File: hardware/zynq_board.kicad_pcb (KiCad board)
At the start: 2 copper layers, 100 x 60 mm, 258 parts, among them J1 USB_OTG, J10 USB_OTG, J6 LSHM-150-xxx-x-DV-A-S, J8 Conn_01x02, J9 Micro_SD_Card_Det_Hirose_DM3AT, Q1 BSS138PS, Q2 BSS138PS, Q3 BSS138PS, U1 xc7z030sbg485, U10 TPS3808G01, U11 MT41K128M8, U13 MT41K128M8, U14 DIFF_OSC, U15 DIFF_OSC, U16 SI53340, U17 NX5P3090, U19 USB3320, U2 SFPP_CONN, U20 OSC, U21 TLK10031, U22 SN74AXC8T245, U23 SN74AXC8T245, U24 SN74AXC8T245, U25 SN74LVC2T45, U26 SN74LVC2T45, U27 SN74LVC2T45, U28 SN74LVC2T45, U29 DMF05LCFLP, U3 TPS8208x, U30 DMF05LCFLP, U31 TC1262-33, U32 MAX14854, U33 CAT24C02TDI-GT3, U34 EMIF06-MSD02N16, U37 SN74LV1T126, U38 SN74LV1T126, U4 TPS8208x, U5 TPSM84424, U6 TPSM84424, U7 TPS8208x, U8 TPS8208x, U9 TPS8208x

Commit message: Started to route DDR3 Memory.
At first added missing Footprint for Reference- and Terminationvoltage Regulator. Added Powerplanes for GND and VCCO. Added decoupling Network to both DDR3 Memory Chips. There are more small caps, to support Memory from other Manufactors.
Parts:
- removed the C142 at (186.5, 141.0)
- removed the C145 at (182.5, 141.0)
- removed D3: LED, LEDs:LED_0402
- removed the D4 at (297.7, 130.4)
- removed the J9 at (183.0, 98.8)
- removed Q2, Q3: BSS138PS, TO_SOT_Packages_SMD:SOT-363_SC-70-6
- removed the R111 at (260.2, 71.4)
- removed the R112 at (260.2, 66.8)
- removed the R113 at (246.2, 80.5)
- removed the R114 at (250.6, 75.8)
- removed R135, R137: 100k, Resistors_SMD:R_0402
- removed R136, R139: 430, Resistors_SMD:R_0402
- added C1: 47µF, Capacitors_SMD:C_1210, F.Cu at (202.2, 69.6)
- added C101: 100 nF, Capacitors_SMD:C_0201, B.Cu at (171.8, 92.6)
- added C102: 100 nF, Capacitors_SMD:C_0201, B.Cu at (174.8, 91.2)
- added C104: 100 nF, Capacitors_SMD:C_0201, B.Cu at (172.0, 98.9)
- added C106: 100 nF, Capacitors_SMD:C_0201, B.Cu at (178.8, 100.0)
- added C107: 100 nF, Capacitors_SMD:C_0201, B.Cu at (173.2, 91.2)
- added C109: 100 nF, Capacitors_SMD:C_0201, B.Cu at (176.0, 97.8)
- added C110: 100 nF, Capacitors_SMD:C_0201, B.Cu at (169.5, 99.4)
- added C111: 100 nF, Capacitors_SMD:C_0201, B.Cu at (176.0, 93.4)
- added C112: 100 nF, Capacitors_SMD:C_0201, B.Cu at (170.8, 91.2)
- added C113: 100 nF, Capacitors_SMD:C_0201, B.Cu at (174.4, 93.6)
- added C114: 10 µF, Capacitors_SMD:C_0603, F.Cu at (183.8, 110.0)
- added C115: 100 nF, Capacitors_SMD:C_0201, B.Cu at (174.8, 105.6)
- added C116: 100 nF, Capacitors_SMD:C_0201, B.Cu at (178.8, 105.6)
- added C117: 100 nF, Capacitors_SMD:C_0201, B.Cu at (173.2, 105.6)
- added C118: 100 nF, Capacitors_SMD:C_0201, B.Cu at (180.4, 105.6)
- added C119: 100 nF, Capacitors_SMD:C_0201, B.Cu at (170.8, 105.6)
- added C120: 100 nF, Capacitors_SMD:C_0201, B.Cu at (176.0, 113.4)
- added C121: 100 nF, Capacitors_SMD:C_0201, B.Cu at (172.0, 113.3)
- added C122: 100 nF, Capacitors_SMD:C_0201, B.Cu at (176.0, 107.8)
- added C123: 100 nF, Capacitors_SMD:C_0201, B.Cu at (168.4, 107.2)
- added C124: 100 nF, Capacitors_SMD:C_0201, B.Cu at (174.4, 108.1)
- added C125: 100 nF, Capacitors_SMD:C_0201, B.Cu at (171.8, 107.0)
- added C126: 100 nF, Capacitors_SMD:C_0201, B.Cu at (174.2, 113.0)
- added C127: 100 nF, Capacitors_SMD:C_0201, B.Cu at (170.4, 112.0)
- added C128: 100 nF, Capacitors_SMD:C_0201, B.Cu at (180.4, 114.4)
- added C129: 100 nF, Capacitors_SMD:C_0201, B.Cu at (169.6, 113.8)
- added C13: 0.47µF, Capacitors_SMD:C_0603, F.Cu at (218.1, 72.0)
- added C130: 100 nF, Capacitors_SMD:C_0201, B.Cu at (173.2, 114.4)
- added C132: 100 nF, Capacitors_SMD:C_0201, B.Cu at (171.6, 114.4)
- added C133: 10µF, Capacitors_SMD:C_0603, F.Cu at (155.3, 128.3)
- added C134: 100 nF, Capacitors_SMD:C_0201, B.Cu at (178.8, 114.4)
- added C136: 10µF, Capacitors_SMD:C_0603, F.Cu at (155.3, 129.5)
- added C137: 0.22µF, Capacitors_SMD:C_0402, F.Cu at (130.0, 145.1)
- added C139: 0.01µF, Capacitors_SMD:C_0402, B.Cu at (150.0, 114.0)
- added C14: 0.47µF, Capacitors_SMD:C_0603, F.Cu at (232.7, 67.1)
- added C140: 0.01µF, Capacitors_SMD:C_0402, B.Cu at (148.2, 98.4)
- added C15: 0.47µF, Capacitors_SMD:C_0603, F.Cu at (212.7, 76.8)
- added C16: 0.47µF, Capacitors_SMD:C_0603, F.Cu at (212.7, 72.0)
- added C17: 0.47µF, Capacitors_SMD:C_0603, F.Cu at (216.4, 62.3)
- added C18: 0.47µF, Capacitors_SMD:C_0603, F.Cu at (203.2, 82.1)
- added C19: 0.47µF, Capacitors_SMD:C_0603, F.Cu at (207.3, 75.5)
- added C20: 0.47µF, Capacitors_SMD:C_0603, F.Cu at (234.4, 72.0)
- added C21: 100µF, Capacitors_SMD:C_1210, F.Cu at (211.2, 63.0)
- added C22: 100µF, Capacitors_SMD:C_1210, F.Cu at (207.0, 69.6)
- added C221: 100 nF, Capacitors_SMD:C_0201, F.Cu at (269.5, 78.6)
- added C222: 100 nF, Capacitors_SMD:C_0201, F.Cu at (275.4, 74.1)
- added C23: 4.7µF, Capacitors_SMD:C_0805, F.Cu at (219.5, 86.5)
- added C231: 1 µF 6,3 V, Capacitors_SMD:C_0402, F.Cu at (338.5, 62.1)
- added C232: 1 µF 6,3 V, Capacitors_SMD:C_0402, F.Cu at (328.7, 78.1)
- added C24: 4.7µF, Capacitors_SMD:C_0805, F.Cu at (224.4, 81.7)
- added C241: 100 nF, Capacitors_SMD:C_0402, F.Cu at (300.8, 122.9)
- added C25: 4.7µF, Capacitors_SMD:C_0805, F.Cu at (228.9, 81.7)
- added C26: 4.7µF, Capacitors_SMD:C_0805, F.Cu at (237.9, 82.4)
- added C27: 0.47µF, Capacitors_SMD:C_0603, F.Cu at (219.5, 81.7)
- added C28: 0.47µF, Capacitors_SMD:C_0603, F.Cu at (227.3, 67.1)
- added C29: 0.47µF, Capacitors_SMD:C_0603, F.Cu at (232.7, 62.3)
- added C3: 47µF, Capacitors_SMD:C_1210, F.Cu at (197.4, 68.7)
- added C30: 0.47µF, Capacitors_SMD:C_0603, F.Cu at (218.1, 76.8)
- added C31: 0.47µF, Capacitors_SMD:C_0603, F.Cu at (223.5, 72.0)
- added C32: 100µF, Capacitors_SMD:C_1210, F.Cu at (153.7, 89.3)
- added C33: 0.47µF, Capacitors_SMD:C_0603, F.Cu at (214.0, 81.7)
- added C34: 47µF, Capacitors_SMD:C_1210, F.Cu at (197.4, 75.3)
- added C35: 0.47µF, Capacitors_SMD:C_0603, F.Cu at (209.1, 86.5)
- added C36: 4.7µF, Capacitors_SMD:C_0805, B.Cu at (157.4, 99.3)
- added C37: 4.7µF, Capacitors_SMD:C_0805, F.Cu at (242.9, 77.3)
- added C38: 0.47µF, Capacitors_SMD:C_0603, B.Cu at (157.1, 97.6)
- added C39: 47µF, Capacitors_SMD:C_1210, F.Cu at (202.2, 76.2)
- added C40: 0.47µF, Capacitors_SMD:C_0603, F.Cu at (223.5, 76.8)
- added C41: 0.47µF, Capacitors_SMD:C_0603, F.Cu at (229.0, 72.0)
- added C42: 0.47µF, Capacitors_SMD:C_0603, F.Cu at (221.9, 62.3)
- added C43: 4.7µF, Capacitors_SMD:C_0805, F.Cu at (243.8, 72.2)
- added C44: 0.47µF, Capacitors_SMD:C_0603, F.Cu at (214.5, 86.5)
- added C45: 4.7µF, Capacitors_SMD:C_0805, F.Cu at (238.4, 77.3)
- added C46: 0.47µF, Capacitors_SMD:C_0603, F.Cu at (238.2, 67.1)
- added C47: 0.47µF, Capacitors_SMD:C_0603, F.Cu at (243.6, 62.3)
- added C48: 100µF, Capacitors_SMD:C_1210, F.Cu at (206.3, 63.0)
- added C49: 0.47µF, Capacitors_SMD:C_0603, F.Cu at (229.0, 76.8)
- added C50: 0.47µF, Capacitors_SMD:C_0603, F.Cu at (203.7, 86.9)
- added C51: 4.7µF, Capacitors_SMD:C_0805, F.Cu at (233.4, 81.9)
- added C52: 0.47µF, Capacitors_SMD:C_0603, F.Cu at (192.8, 87.7)
- added C53: 0.47µF, Capacitors_SMD:C_0603, F.Cu at (197.8, 82.1)
- added C54: 100µF, Capacitors_SMD:C_1210, F.Cu at (192.6, 81.9)
- added C56: 4.7µF, Capacitors_SMD:C_0805, F.Cu at (243.1, 67.1)
- added C57: 0.47µF, Capacitors_SMD:C_0603, F.Cu at (216.4, 67.1)
- added C85: 1 µF 6.3 V, Capacitors_SMD:C_0402, F.Cu at (310.9, 92.2)
- added C86: 1 µF 6.3 V, Capacitors_SMD:C_0402, F.Cu at (302.0, 99.1)
- added C87: 10 µF, Capacitors_SMD:C_0603, F.Cu at (183.8, 95.8)
- added C89: 100 nF, Capacitors_SMD:C_0201, B.Cu at (170.4, 97.6)
- added C91: 100 nF, Capacitors_SMD:C_0201, B.Cu at (180.4, 91.2)
- added C92: 100 nF, Capacitors_SMD:C_0201, B.Cu at (168.4, 92.8)
- added C94: 100 nF, Capacitors_SMD:C_0201, B.Cu at (178.8, 91.2)
- added C95: 100 nF, Capacitors_SMD:C_0201, B.Cu at (171.6, 100.0)
- added C97: 100 nF, Capacitors_SMD:C_0201, B.Cu at (174.2, 98.7)
- added C98: 100 nF, Capacitors_SMD:C_0201, B.Cu at (173.2, 100.0)
- added C99: 100 nF, Capacitors_SMD:C_0201, B.Cu at (180.4, 100.0)
- added D1: LED_Small, LEDs:LED_0402, F.Cu at (268.6, 69.7)
- added D2: LED_Small, LEDs:LED_0402, F.Cu at (257.1, 77.4)
- added D6: 15 V, Diodes_SMD:D_SOD-123, F.Cu at (324.3, 138.0)
- added D7: TN1515-600B-TR, TO_SOT_Packages_SMD:TO-252-2, F.Cu at (100.8, 63.6)
- added F1: Fuse, Resistors_SMD:R_0402, F.Cu at (328.6, 137.4)
- added J10: DM3CS, footprints:DM3CS, F.Cu at (124.0, 103.4)
- added J12: Conn_01x02, footprints:WAGO-890-802, F.Cu at (89.7, 67.8)
- added J6: MDR20, footprints:Conn_MDR20, F.Cu at (74.5, 97.9)
- added L1: 120 Ohm @ 1Mhz, Inductors_SMD:L_0603, F.Cu at (196.9, 62.7)
- added R119: 300, Resistors_SMD:R_0402, F.Cu at (282.4, 82.0)
- added R120: 300, Resistors_SMD:R_0402, F.Cu at (286.4, 76.1)
- added R121: 200k, Resistors_SMD:R_0402, F.Cu at (282.4, 77.4)
- added R122: 200k, Resistors_SMD:R_0402, F.Cu at (293.9, 66.8)
- added R123: 1k, Resistors_SMD:R_0402, F.Cu at (298.5, 62.1)
- added R124: 1k, Resistors_SMD:R_0402, F.Cu at (275.5, 83.3)
- added R125: 1k, Resistors_SMD:R_0402, F.Cu at (289.8, 71.4)
- added R126: 1k, Resistors_SMD:R_0402, F.Cu at (271.5, 83.3)
- added R159: 40,2, Resistors_SMD:R_0402, F.Cu at (313.7, 120.0)
- added R40: 10kΩ, Resistors_SMD:R_0402, F.Cu at (162.7, 129.8)
- added R41: 10kΩ, Resistors_SMD:R_0402, F.Cu at (162.7, 128.8)
- added R78: 4k7, Resistors_SMD:R_0402, F.Cu at (349.8, 71.6)
- added R79: 4k7, Resistors_SMD:R_0402, F.Cu at (352.9, 71.6)
- added U11: MCP1700-2502E_SOT23, TO_SOT_Packages_SMD:SOT-23, F.Cu at (297.4, 93.5)
- added U13: TPS51206, footprints:TI_PWSON-N10_2.0x2.0mm, F.Cu at (159.2, 128.6)
- added U19: SMP1255PUTG, footprints:SMC_MicroDFN_1.8x2.0mm_0.4mm_Pitch, F.Cu at (290.0, 136.3)
- added U26: LSF0102, footprints:TI-DQE_PX2SON-N8_1.4x1mm_0.35mm_Pitch, F.Cu at (256.5, 80.5)
- added U27: LSF0102, footprints:TI-DQE_PX2SON-N8_1.4x1mm_0.35mm_Pitch, F.Cu at (279.4, 60.6)
- added U38: 33.333MHZ, footprints:ASDMB_2.5x2.0mm_1.65mm_pitch, F.Cu at (292.4, 125.6)
- added U39: SMP1255PUTG, footprints:SMC_MicroDFN_1.8x2.0mm_0.4mm_Pitch, F.Cu at (248.4, 103.5)
- added U40: FT234XD, Housings_DFN_QFN:DFN-12-1EP_3x3mm_Pitch0.45mm, F.Cu at (268.0, 100.0)
- C11: value 47µF -> 4.7µF; footprint Capacitors_SMD:C_1210 -> Capacitors_SMD:C_0805
- C12: value 100µF -> 0.47µF; footprint Capacitors_SMD:C_1210 -> Capacitors_SMD:C_0603
- C131: renamed from C48; moved to B.Cu
- C138: renamed from C53; moved to B.Cu
- C4, C6: value 0.47µF -> 4.7µF; footprint Capacitors_SMD:C_0603 -> Capacitors_SMD:C_0805
- C7: value 0.47µF -> 100µF; footprint Capacitors_SMD:C_0603 -> Capacitors_SMD:C_1210
- C9: value 4.7µF -> 0.47µF; footprint Capacitors_SMD:C_0805 -> Capacitors_SMD:C_0603
- J7: renamed from J6; moved to B.Cu
- Q1: value BSS138PS -> DMP3056L; footprint TO_SOT_Packages_SMD:SOT-363_SC-70-6 -> TO_SOT_Packages_SMD:SOT-23
- R115, R116: value 10k -> 420
- R117, R118: value 10k -> 300
- U35: renamed from U32; moved to B.Cu
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- renumbered C2 to C10, C44 to C100, C45 to C103, C46 to C105, C47 to C108, C50 to C135, C54 to C141, C55 to C142, C56 to C143, C57 to C144, C58 to C145, C59 to C146, C60 to C147, C61 to C148, C62 to C149, C63 to C150, C64 to C151, C65 to C152, C66 to C153, C67 to C154, C68 to C155, C69 to C156, C70 to C157, C71 to C158, C72 to C159, C73 to C160, C74 to C161, C75 to C162, C76 to C163, C77 to C164, C78 to C165, C79 to C166, C80 to C167, C81 to C168, C82 to C169, C83 to C170, C84 to C171, C85 to C172, C86 to C173, C87 to C174, C88 to C175, C89 to C176, C90 to C177, C91 to C178, C92 to C179, C93 to C180, C94 to C181, C95 to C182, C96 to C183, C97 to C184, C98 to C185, C99 to C186, C100 to C187, C101 to C188, C102 to C189, C103 to C190, C104 to C191, C105 to C192, C106 to C193, C107 to C194, C108 to C195, C109 to C196, C110 to C197, C111 to C198, C112 to C199, C113 to C200, C114 to C201, C115 to C202, C116 to C203, C117 to C204, C118 to C205, C119 to C206, C120 to C207, C121 to C208, C122 to C209, C123 to C210, C124 to C211, C125 to C212, C126 to C213, C127 to C214, C128 to C215, C129 to C216, C130 to C217, C131 to C218, C132 to C219, C133 to C220, C150 to C239, C151 to C240, C153 to C243, C154 to C244, C155 to C245, C156 to C246, C157 to C247, C158 to C248, C159 to C249, C160 to C250, C161 to C251, C3 to C5, C10 to C55, C8 to C58, C14 to C59, C15 to C60, C16 to C61, C17 to C62, C18 to C63, C19 to C64, C5 to C8, C40 to C88, C41 to C90, C42 to C93, C43 to C96, D2 to D4, J10 to J11, J8 to J9, R96 to R100, R97 to R101, R98 to R102, R99 to R103, R100 to R104, R101 to R105, R102 to R106, R103 to R107, R104 to R108, R105 to R109, R106 to R110, R107 to R111, R108 to R112, R109 to R113, R110 to R114, R138 to R142, R134 to R143, R140 to R144, R141 to R145, R142 to R146, R143 to R147, R144 to R148, R145 to R149, R146 to R150, R147 to R151, R148 to R152, R149 to R153, R150 to R154, R151 to R155, R152 to R156, R153 to R157, R154 to R158, R156 to R161, R157 to R162, R158 to R163, R159 to R164, R160 to R165, R66 to R68, R67 to R69, R68 to R70, R69 to R71, R70 to R72, R71 to R73, R72 to R74, R73 to R75, R74 to R76, R76 to R80, R77 to R81, R78 to R82, R79 to R83, R80 to R84, R81 to R85, R82 to R86, R83 to R87, R84 to R88, R85 to R89, R86 to R90, R87 to R91, R88 to R92, R89 to R93, R90 to R94, R91 to R95, R92 to R96, R93 to R97, R94 to R98, R95 to R99, U11 to U12, U13 to U14, U14 to U15, U15 to U16, U16 to U17, U17 to U18, U19 to U20, U20 to U21, U21 to U22, U22 to U23, U23 to U24, U24 to U25, U25 to U28, U26 to U29, U27 to U30, U28 to U31, U29 to U32, U30 to U33, U31 to U34, U33 to U36, U34 to U37, U37 to U41, U38 to U42
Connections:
- C10 pad 1: (no net) -> +1V0
- C10 pad 2: (no net) -> GND
- C100 pad 1: +1V5 -> VCCO_DDR
- C103 pad 1: +1V5 -> VCCO_DDR
- C105 pad 1: +1V5 -> VCCO_DDR
- C108 pad 1: +1V5 -> VCCO_DDR
- C11 pad 1: (no net) -> +1V0
- C11 pad 2: (no net) -> GND
- C12 pad 1: (no net) -> VCCO_13
- C12 pad 2: (no net) -> GND
- C131 pad 1: /DDR/VTT_REF -> /DDR/VREF
- C138 pad 1: /DDR/VTT_REF -> /DDR/VREF
- C141 pad 1: +3V3 -> VCCO_MIO0
- C142 pad 1: +3V3 -> VCCO_MIO0
- C145 pad 1: +3V3 -> VCCO_MIO0
- C148 pad 1: +3V3 -> VCCO_MIO0
- C149 pad 1: +1V8 -> VCCO_34
- C150 pad 1: +1V8 -> VCCO_34
- C151 pad 1: +3V3 -> VCCO_MIO0
- C152 pad 1: +1V8 -> VCCO_34
- C215 pad 1: +1V8 -> VCCO_34
- C216 pad 1: +1V8 -> VCCO_34
- C217 pad 1: +1V8 -> VCCO_34
- C218 pad 1: +3V3 -> VCCO_MIO0
- C219 pad 1: +3V3 -> VCCO_MIO0
- C220 pad 1: +3V3 -> VCCO_MIO0
- C239 pad 2: +3V3 -> VCCO_MIO0
- C240 pad 2: +3V3 -> VCCO_MIO0
- C250 pad 1: +3V3 -> VCCO_MIO0
- C4 pad 1: (no net) -> VCCO_13
- C4 pad 2: (no net) -> GND
- C5 pad 1: (no net) -> +1V0
- C5 pad 2: (no net) -> GND
- C55 pad 1: (no net) -> /Power/VCC_PLL
- C55 pad 2: (no net) -> GND
- C58 pad 1: (no net) -> /Power/VCC_PLL
- C58 pad 2: (no net) -> GND
- C59 pad 1: +3V3 -> VCCO_MIO0
- C6 pad 1: (no net) -> VCCO_13
- C6 pad 2: (no net) -> GND
- C60 pad 1: +3V3 -> VCCO_MIO0
- C7 pad 1: (no net) -> +1V0
- C7 pad 2: (no net) -> GND
- C8 pad 1: (no net) -> +1V0
- C8 pad 2: (no net) -> GND
- C88 pad 1: +1V5 -> VCCO_DDR
- C9 pad 1: (no net) -> VCCO_13
- C9 pad 2: (no net) -> GND
- C90 pad 1: +1V5 -> VCCO_DDR
- C93 pad 1: +1V5 -> VCCO_DDR
- C96 pad 1: +1V5 -> VCCO_DDR
- J11 pad 4: (no net) -> Net-(J11-Pad4)
- J7 pad 10: /Camera Connector/CAM_CTRL_0_N -> /Levelshifters/CAM_SPI_MISO
- J7 pad 100: /Camera Connector/D12_P -> GND
- J7 pad 12: GND -> /Levelshifters/CAM_SPI_MOSI
- J7 pad 14: /Camera Connector/D0_N -> /Camera Connector/T_EXP2_1
- J7 pad 15: +5V -> /IMU_EN_1
- J7 pad 16: /Camera Connector/D0_P -> /Camera Connector/T_EXP1_1
- J7 pad 17: /Camera Connector/IMU_SPI_EN_1 -> /IMU_EN_0
- J7 pad 18: GND -> /Camera Connector/FRAME_REQ_1
- J7 pad 19: /Camera Connector/IMU_SPI_EN_0 -> /IMU_CLK
- J7 pad 2: /Camera Connector/CAM_CLK_0_P -> /Levelshifters/CAM_RESET
- J7 pad 20: /Camera Connector/D1_N -> /Camera Connector/T_EXP2_0
- J7 pad 21: /Camera Connector/IMU_SPI_CLK -> /IMU_MOSI
- J7 pad 22: /Camera Connector/D1_P -> /Camera Connector/T_EXP1_0
- J7 pad 23: /Camera Connector/IMU_SPI_MOSI -> /IMU_MISO
- J7 pad 24: GND -> /Camera Connector/FRAME_REQ_0
- J7 pad 25: /Camera Connector/IMU_SPI_MISO -> /IMU_FRAME_GPIO0
- J7 pad 26: /Camera Connector/D2_N -> GND
- J7 pad 27: /IMU_FRAME_GPIO0 -> /IMU_INT1_GPIO1
- J7 pad 28: /Camera Connector/D2_P -> /Levelshifters/CAM1_CLK_REF
- J7 pad 29: /IMU_INT1_GPIO1 -> /IMU_INT2_GPIO2
- J7 pad 31: /IMU_INT2_GPIO2 -> /Levelshifters/CAM_SCL
- J7 pad 32: /Camera Connector/D3_N -> /Levelshifters/CAM0_CLK_REF
- J7 pad 33: GND -> /Levelshifters/CAM_SDA
- J7 pad 34: /Camera Connector/D3_P -> GND
- J7 pad 35: /Levelshifters/CAM1_CLK_REF -> GND
- J7 pad 36: GND -> /Camera Connector/CAM_CTRL_0_N
- J7 pad 37: GND -> /Camera Connector/LVDS_CLK0_P
- J7 pad 38: /Camera Connector/D4_N -> /Camera Connector/CAM_CTRL_0_P
- J7 pad 39: /Levelshifters/CAM0_CLK_REF -> /Camera Connector/LVDS_CLK0_N
- J7 pad 4: /Camera Connector/CAM_CLK_0_N -> /Levelshifters/CAM_SPI_CLK
- J7 pad 40: /Camera Connector/D4_P -> GND
- J7 pad 42: GND -> /Camera Connector/D1_N
- J7 pad 43: /Levelshifters/CAM_SCL -> /Camera Connector/D0_N
- J7 pad 44: /Camera Connector/D5_N -> /Camera Connector/D1_P
- J7 pad 45: /Levelshifters/CAM_SDA -> /Camera Connector/D0_P
- J7 pad 46: /Camera Connector/D5_P -> GND
- J7 pad 47: /Levelshifters/CAM_RESET -> GND
- J7 pad 48: GND -> /Camera Connector/D3_N
- J7 pad 49: /Levelshifters/CAM_SPI_EN_1 -> /Camera Connector/D4_N
- J7 pad 50: /Camera Connector/D6_N -> /Camera Connector/D3_P
- J7 pad 51: /Levelshifters/CAM_SPI_EN_0 -> /Camera Connector/D4_P
- J7 pad 52: /Camera Connector/D6_P -> GND
- J7 pad 53: /Levelshifters/CAM_SPI_CLK -> GND
- J7 pad 54: GND -> /Camera Connector/D2_N
- J7 pad 55: /Levelshifters/CAM_SPI_MISO -> /Camera Connector/D5_N
- J7 pad 56: /Camera Connector/D7_N -> /Camera Connector/D2_P
- J7 pad 57: /Levelshifters/CAM_SPI_MOSI -> /Camera Connector/D5_P
- J7 pad 58: /Camera Connector/D7_P -> GND
- J7 pad 59: /Camera Connector/T_EXP2_1 -> GND
- J7 pad 6: GND -> /Levelshifters/CAM_SPI_EN_1
- J7 pad 60: GND -> /Camera Connector/D7_N
- J7 pad 61: /Camera Connector/T_EXP1_1 -> /Camera Connector/CAM_CTRL_1_P
- J7 pad 62: /Camera Connector/CAM_CLK_1_P -> /Camera Connector/D7_P
- J7 pad 63: /Camera Connector/FRAME_REQ_1 -> /Camera Connector/CAM_CTRL_1_N
- J7 pad 64: /Camera Connector/CAM_CLK_1_N -> GND
- J7 pad 65: /Camera Connector/T_EXP2_0 -> GND
- J7 pad 66: GND -> /Camera Connector/LVDS_CLK1_N
- J7 pad 67: /Camera Connector/T_EXP1_0 -> /Camera Connector/D10_N
- J7 pad 68: /Camera Connector/CAM_CTRL_1_P -> /Camera Connector/LVDS_CLK1_P
- J7 pad 69: /Camera Connector/FRAME_REQ_0 -> /Camera Connector/D10_P
- J7 pad 70: /Camera Connector/CAM_CTRL_1_N -> GND
- J7 pad 72: GND -> /Camera Connector/D8_N
- J7 pad 73: /Camera Connector/LVDS_CLK1_P -> /Camera Connector/D11_N
- J7 pad 74: /Camera Connector/D8_N -> /Camera Connector/D8_P
- J7 pad 75: /Camera Connector/LVDS_CLK1_N -> /Camera Connector/D11_P
- J7 pad 76: /Camera Connector/D8_P -> GND
- J7 pad 78: GND -> /Camera Connector/D6_N
- J7 pad 79: /Camera Connector/LVDS_CLK0_P -> /Camera Connector/D13_N
- J7 pad 8: /Camera Connector/CAM_CTRL_0_P -> /Levelshifters/CAM_SPI_EN_0
- J7 pad 80: /Camera Connector/D9_N -> /Camera Connector/D6_P
- J7 pad 81: /Camera Connector/LVDS_CLK0_N -> /Camera Connector/D13_P
- J7 pad 82: /Camera Connector/D9_P -> GND
- J7 pad 84: GND -> /Camera Connector/D9_N
- J7 pad 85: /Camera Connector/D15_P -> /Camera Connector/D15_N
- J7 pad 86: /Camera Connector/D10_N -> /Camera Connector/D9_P
- J7 pad 87: /Camera Connector/D15_N -> /Camera Connector/D15_P
- J7 pad 88: /Camera Connector/D10_P -> GND
- J7 pad 90: GND -> /Camera Connector/D12_N
- J7 pad 91: /Camera Connector/D14_P -> /Camera Connector/D14_N
- J7 pad 92: /Camera Connector/D11_N -> /Camera Connector/D12_P
- J7 pad 93: /Camera Connector/D14_N -> /Camera Connector/D14_P
- J7 pad 94: /Camera Connector/D11_P -> GND
- J7 pad 96: GND -> /Camera Connector/CAM_CLK_0_N
- J7 pad 97: /Camera Connector/D13_P -> /Camera Connector/CAM_CLK_1_N
- J7 pad 98: /Camera Connector/D12_N -> /Camera Connector/CAM_CLK_0_P
- J7 pad 99: /Camera Connector/D13_N -> /Camera Connector/CAM_CLK_1_P
- Q1 pad 1: /Levelshifters/CAM_SCL_18 -> GND
- Q1 pad 2: +1V8 -> /V_IN
- Q1 pad 3: /Levelshifters/CAM_SDA -> Net-(D6-Pad1)
- R1 pad 1: +3V3 -> VCCO_MIO0
- R102 pad 1: +1V8 -> VCCO_34
- R106 pad 1: +1V8 -> VCCO_34
- R109 pad 1: +1V8 -> VCCO_34
- R113 pad 1: +1V8 -> VCCO_34
- R115 pad 1: +3V3 -> Net-(D1-Pad2)
- R115 pad 2: /Levelshifters/CAM_SCL -> Net-(R115-Pad2)
- R116 pad 1: +3V3 -> Net-(D2-Pad2)
- R116 pad 2: /Levelshifters/CAM_SDA -> Net-(R116-Pad2)
- R117 pad 1: +3V3 -> VCCO_34
- R117 pad 2: /SFP_SCL -> /Levelshifters/SFP_SCL_18
- R118 pad 1: +3V3 -> VCCO_34
- R118 pad 2: /SFP_SDA -> /Levelshifters/CAM_SCL_18
- R142 pad 1: +1V8 -> (no net)
- R143 pad 1: +3V3 -> VCCO_MIO0
- R144 pad 1: +3V3 -> VCCO_MIO0
- R145 pad 1: +3V3 -> VCCO_MIO0
- R146 pad 1: +3V3 -> VCCO_MIO0
- R147 pad 1: +3V3 -> VCCO_MIO0
- R149 pad 1: +3V3 -> VCCO_MIO0
- R151 pad 1: +3V3 -> VCCO_MIO0
- R153 pad 1: +3V3 -> VCCO_MIO0
- R155 pad 1: +3V3 -> VCCO_MIO0
- R162 pad 2: (no net) -> Net-(R162-Pad2)
- R163 pad 1: (no net) -> Net-(R163-Pad1)
- R165 pad 1: +3V3 -> VCCO_MIO0
- R3 pad 1: +3V3 -> VCCO_MIO0
- R4 pad 1: +3V3 -> VCCO_MIO0
- R6 pad 1: +3V3 -> VCCO_MIO0
- R7 pad 1: +3V3 -> VCCO_MIO0
- R70 pad 2: +3V3 -> VCCO_MIO0
- R74 pad 1: +1V8 -> VCCO_34
- R8 pad 1: +3V3 -> VCCO_MIO0
- R82 pad 1: +1V8 -> VCCO_34
- R84 pad 1: +1V8 -> VCCO_34
- R86 pad 1: +1V8 -> VCCO_34
- R88 pad 1: +1V8 -> VCCO_34
- R9 pad 1: +3V3 -> VCCO_MIO0
- R90 pad 1: +1V8 -> VCCO_34
- R92 pad 1: +1V8 -> VCCO_34
- R94 pad 1: +1V8 -> VCCO_34
- R96 pad 2: +1V8 -> VCCO_34
- R97 pad 2: +1V8 -> VCCO_34
- U1 pad A13: +3V3 -> VCCO_MIO0
- U1 pad A3: Net-(U1-PadA3) -> VCCO_34
- U1 pad A6: /Camera Connector/IMU_SPI_MISO -> /IMU_MISO
- U1 pad A7: /Camera Connector/IMU_SPI_CLK -> /IMU_CLK
- U1 pad AA13: Net-(U1-PadAA13) -> VCCO_13
- U1 pad AB20: Net-(U1-PadAA13) -> VCCO_13
- U1 pad B10: +3V3 -> VCCO_MIO0
- U1 pad B20: +3V3 -> VCCO_MIO0
- U1 pad B6: /Camera Connector/IMU_SPI_MOSI -> /IMU_MOSI
- U1 pad B7: /Camera Connector/IMU_SPI_EN_0 -> /IMU_EN_0
- U1 pad B8: /Camera Connector/IMU_SPI_EN_1 -> /IMU_EN_1
- U1 pad C17: +3V3 -> VCCO_MIO0
- U1 pad C7: Net-(U1-PadA3) -> VCCO_34
- U1 pad D14: +3V3 -> VCCO_MIO0
- U1 pad D4: Net-(U1-PadA3) -> VCCO_34
- U1 pad E1: Net-(U1-PadA3) -> VCCO_34
- U1 pad E11: +3V3 -> VCCO_MIO0
- U1 pad E21: Net-(U1-PadE21) -> VCCO_DDR
- U1 pad F16: (no net) -> /Processing System IO/CLK_33.33
- U1 pad F18: Net-(U1-PadE21) -> VCCO_DDR
- U1 pad F8: Net-(U1-PadA3) -> VCCO_34
- U1 pad G12: (no net) -> GND
- U1 pad G13: (no net) -> /Power/VCC_PLL
- U1 pad G14: (no net) -> GND
- U1 pad G5: Net-(U1-PadA3) -> VCCO_34
- U1 pad H16: (no net) -> /DDR/VREF
- U1 pad H2: Net-(U1-PadH2) -> VCCO_34
- U1 pad H22: Net-(U1-PadE21) -> VCCO_DDR
- U1 pad J19: Net-(U1-PadE21) -> VCCO_DDR
- U1 pad K11: (no net) -> GND
- U1 pad K12: (no net) -> VCCO_34
- U1 pad K14: +1V8 -> VCCO_34
- U1 pad K16: Net-(U1-PadE21) -> VCCO_DDR
- U1 pad K6: Net-(U1-PadH2) -> VCCO_34
- U1 pad L11: (no net) -> GND
- U1 pad L12: (no net) -> GND
- U1 pad L13: +1V8 -> VCCO_34
- U1 pad L3: Net-(U1-PadH2) -> VCCO_34
- U1 pad M11: (no net) -> GND
- U1 pad M12: (no net) -> GND
- U1 pad M14: +1V8 -> VCCO_34
- U1 pad M20: Net-(U1-PadE21) -> VCCO_DDR
- U1 pad N11: (no net) -> GND
- U1 pad N12: (no net) -> GND
- U1 pad N13: +1V8 -> VCCO_34
- U1 pad N17: Net-(U1-PadE21) -> VCCO_DDR
- U1 pad N7: Net-(U1-PadH2) -> VCCO_34
- U1 pad P12: +1V8 -> VCCO_34
- U1 pad P14: +1V8 -> VCCO_34
- U1 pad P16: (no net) -> /DDR/VREF
- U1 pad P4: Net-(U1-PadH2) -> VCCO_34
- U1 pad R1: Net-(U1-PadH2) -> VCCO_34
- U1 pad R11: (no net) -> VCCO_34
- U1 pad R13: +1V8 -> VCCO_34
- U1 pad R21: Net-(U1-PadE21) -> VCCO_DDR
- U1 pad T11: (no net) -> VCCO_34
- U1 pad T12: +1V8 -> VCCO_34
- U1 pad T14: (no net) -> VCCO_34
- U1 pad T15: (no net) -> VCCO_34
- U1 pad T18: Net-(U1-PadAA13) -> VCCO_13
- U1 pad T8: (no net) -> Net-(R78-Pad2)
- U1 pad T9: (no net) -> GND
- U1 pad U15: Net-(U1-PadAA13) -> VCCO_13
- U1 pad V10: (no net) -> Net-(R79-Pad2)
- U1 pad V12: Net-(U1-PadAA13) -> VCCO_13
- U1 pad V22: Net-(U1-PadE21) -> VCCO_DDR
- U1 pad W19: Net-(U1-PadAA13) -> VCCO_13
- U1 pad Y16: Net-(U1-PadAA13) -> VCCO_13
- U12 pad A1: +1V5 -> VCCO_DDR
- U12 pad A8: +1V5 -> VCCO_DDR
- U12 pad B2: +1V5 -> VCCO_DDR
- U12 pad C1: +1V5 -> VCCO_DDR
- U12 pad C9: +1V5 -> VCCO_DDR
- U12 pad D2: +1V5 -> VCCO_DDR
- U12 pad D9: +1V5 -> VCCO_DDR
- U12 pad E9: +1V5 -> VCCO_DDR
- U12 pad F1: +1V5 -> VCCO_DDR
- U12 pad G7: +1V5 -> VCCO_DDR
- U12 pad H1: /DDR/VTT_REF -> /DDR/VREF
- U12 pad H2: +1V5 -> VCCO_DDR
- U12 pad H9: +1V5 -> VCCO_DDR
- U12 pad K2: +1V5 -> VCCO_DDR
- U12 pad K8: +1V5 -> VCCO_DDR
- U12 pad M8: /DDR/VTT_REF -> /DDR/VREF
- U12 pad N1: +1V5 -> VCCO_DDR
- U12 pad N9: +1V5 -> VCCO_DDR
- U12 pad R1: +1V5 -> VCCO_DDR
- U12 pad R9: +1V5 -> VCCO_DDR
- U14 pad A1: +1V5 -> VCCO_DDR
- U14 pad A8: +1V5 -> VCCO_DDR
- U14 pad B2: +1V5 -> VCCO_DDR
- U14 pad C1: +1V5 -> VCCO_DDR
- U14 pad C9: +1V5 -> VCCO_DDR
- U14 pad D2: +1V5 -> VCCO_DDR
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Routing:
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- added copper zone on GND1.Cu, net GND
- added copper zone on GND6.Cu, net GND
- added copper zone on PWR3.Cu, net VCCO_DDR
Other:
- board size 100 x 60 mm -> 120 x 75 mm
- copper layers 2 -> 8
- net class PWR_DDR added: clearance 0.1, trace_width 0.3, via_dia 0.4, via_drill 0.2
- rule pad_to_mask_clearance: 0.2 -> 0.05
- board text added: "VDD"
- board text added: "VDDQ"

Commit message: Routed DDR3 Memory. Not length matched yet. Also V_TT and V_Ref is WIP. Changed Footprint for FPGA to match more Xilinx' Specs(and to ease routing).
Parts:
- added C252: 100 µF, Capacitors_SMD:C_1210, F.Cu at (172.4, 128.1)
- added C253: 100 µF, Capacitors_SMD:C_1210, F.Cu at (175.9, 128.1)
- added C254: 4,7 µF, Capacitors_SMD:C_0402, B.Cu at (183.0, 118.5)
- added C255: 4,7 µF, Capacitors_SMD:C_0402, F.Cu at (176.0, 121.5)
- added C256: 10 nF, Capacitors_SMD:C_0201, F.Cu at (175.0, 121.5)
- added C257: 10 nF, Capacitors_SMD:C_0201, F.Cu at (185.0, 118.5)
- added C258: 10 nF, Capacitors_SMD:C_0201, F.Cu at (185.0, 121.5)
- added C259: 10 nF, Capacitors_SMD:C_0201, F.Cu at (175.0, 118.5)
- added R166: 40.2Ω, Resistors_SMD:R_0402, F.Cu at (179.0, 118.5)
- added R167: 40.2Ω, Resistors_SMD:R_0402, F.Cu at (181.0, 121.5)
- added R168: 40.2Ω, Resistors_SMD:R_0402, F.Cu at (183.0, 121.5)
- added R43: 40.2Ω, Resistors_SMD:R_0402, B.Cu at (181.0, 118.5)
- added R44: 40.2Ω, Resistors_SMD:R_0402, F.Cu at (182.0, 118.5)
- added R45: 40.2Ω, Resistors_SMD:R_0402, B.Cu at (178.0, 118.5)
- added R46: 40.2Ω, Resistors_SMD:R_0402, B.Cu at (180.0, 118.5)
- added R47: 40.2Ω, Resistors_SMD:R_0402, B.Cu at (179.0, 118.5)
- added R48: 40.2Ω, Resistors_SMD:R_0402, B.Cu at (177.0, 118.5)
- added R49: 40.2Ω, Resistors_SMD:R_0402, F.Cu at (180.0, 118.5)
- added R50: 40.2Ω, Resistors_SMD:R_0402, F.Cu at (179.0, 121.5)
- added R51: 40.2Ω, Resistors_SMD:R_0402, B.Cu at (176.0, 118.5)
- added R52: 4.7 kΩ, Resistors_SMD:R_0402, F.Cu at (183.7, 113.3)
- added R53: 80.6Ω, Resistors_SMD:R_0402, B.Cu at (176.4, 109.9)
- added R54: 40.2Ω, Resistors_SMD:R_0402, F.Cu at (184.0, 118.5)
- added R55: 40.2Ω, Resistors_SMD:R_0402, F.Cu at (178.0, 118.5)
- added R56: 40.2Ω, Resistors_SMD:R_0402, F.Cu at (177.0, 118.5)
- added R57: 40.2Ω, Resistors_SMD:R_0402, B.Cu at (182.0, 118.5)
- added R58: 40.2Ω, Resistors_SMD:R_0402, F.Cu at (183.0, 118.5)
- added R59: 40.2Ω, Resistors_SMD:R_0402, F.Cu at (181.0, 118.5)
- added R60: 40.2Ω, Resistors_SMD:R_0402, F.Cu at (184.0, 121.5)
- added R61: 40.2Ω, Resistors_SMD:R_0402, F.Cu at (182.0, 121.5)
- added R62: 40.2Ω, Resistors_SMD:R_0402, F.Cu at (177.0, 121.5)
- added R63: 40.2Ω, Resistors_SMD:R_0402, F.Cu at (180.0, 121.5)
- added R64: 40.2Ω, Resistors_SMD:R_0402, F.Cu at (176.0, 118.5)
- added R65: 40.2Ω, Resistors_SMD:R_0402, F.Cu at (178.0, 121.5)
- added R66: 80.6Ω, Resistors_SMD:R_0402, F.Cu at (203.4, 121.4)
- added R67: 80.6Ω, Resistors_SMD:R_0402, F.Cu at (198.6, 121.4)
- added REF**: MountingHole_3.2mm_M3, Mounting_Holes:MountingHole_3.2mm_M3, F.Cu at (202.2, 97.1)
- added REF**: MountingHole_3.2mm_M3, Mounting_Holes:MountingHole_3.2mm_M3, F.Cu at (146.0, 80.0)
- added REF**: MountingHole_3.2mm_M3, Mounting_Holes:MountingHole_3.2mm_M3, F.Cu at (115.0, 80.0)
- added REF**: MountingHole_3.2mm_M3, Mounting_Holes:MountingHole_3.2mm_M3, F.Cu at (186.0, 131.0)
- added REF**: MountingHole_3.2mm_M3, Mounting_Holes:MountingHole_3.2mm_M3, F.Cu at (74.0, 131.0)
- added REF**: MountingHole_3.2mm_M3, Mounting_Holes:MountingHole_3.2mm_M3, F.Cu at (74.0, 64.0)
- added REF**: MountingHole_3.2mm_M3, Mounting_Holes:MountingHole_3.2mm_M3, F.Cu at (186.0, 64.0)
- C36, C38: moved to F.Cu
- moved R95 446.1 mm to (-169.1, 122.3)
- moved R99 442.7 mm to (-162.7, 123.1)
- moved C208 435.3 mm to (-179.3, 104.3)
- moved C203 435.0 mm to (-179.3, 113.2)
- moved C202 434.9 mm to (-173.6, 108.7)
- moved C201 434.8 mm to (-167.9, 104.3)
- moved R144 432.1 mm to (-122.6, 116.7)
- moved R159 432.1 mm to (-118.4, 118.7)
- moved R157 432.0 mm to (-114.3, 118.7)
- moved R104 432.0 mm to (-154.9, 118.6)
- moved R100 431.9 mm to (-159.1, 123.1)
- moved R90 431.9 mm to (-157.7, 108.8)
- moved R91 431.2 mm to (-165.9, 122.6)
- moved C213 430.8 mm to (-154.9, 123.3)
- moved C200 429.7 mm to (-179.3, 117.7)
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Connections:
- U1 pad M16: (no net) -> Net-(R66-Pad1)
- U1 pad N16: (no net) -> Net-(R67-Pad2)
- U12 pad A2: /DDR/DQ13 -> /DDR/DQ11
- U12 pad A3: /DDR/DQ15 -> /DDR/DQ10
- U12 pad A7: /DDR/DQ12 -> /DDR/DQ14
- U12 pad B8: /DDR/DQ14 -> /DDR/DQ9
- U12 pad C2: /DDR/DQ11 -> /DDR/DQ13
- U12 pad C3: /DDR/DQ9 -> /DDR/DQ12
- U12 pad C8: /DDR/DQ10 -> /DDR/DQ15
- U12 pad E3: /DDR/DQ0 -> /DDR/DQ6
- U12 pad F2: /DDR/DQ2 -> /DDR/DQ7
- U12 pad F8: /DDR/DQ3 -> /DDR/DQ2
- U12 pad G2: /DDR/DQ6 -> /DDR/DQ5
- U12 pad H7: /DDR/DQ7 -> /DDR/DQ0
- U12 pad H8: /DDR/DQ5 -> /DDR/DQ3
- U14 pad A2: /DDR/DQ29 -> /DDR/DQ31
- U14 pad A3: /DDR/DQ31 -> /DDR/DQ29
- U14 pad B8: /DDR/DQ30 -> /DDR/DQ27
- U14 pad C2: /DDR/DQ27 -> /DDR/DQ24
- U14 pad C3: /DDR/DQ25 -> /DDR/DQ26
- U14 pad C8: /DDR/DQ26 -> /DDR/DQ30
- U14 pad D7: /DDR/DQ24 -> /DDR/DQ25
- U14 pad E3: /DDR/DQ16 -> /DDR/DQ21
- U14 pad F2: /DDR/DQ18 -> /DDR/DQ20
- U14 pad F7: /DDR/DQ17 -> /DDR/DQ22
- U14 pad F8: /DDR/DQ19 -> /DDR/DQ18
- U14 pad G2: /DDR/DQ22 -> /DDR/DQ19
- U14 pad H3: /DDR/DQ20 -> /DDR/DQ17
- U14 pad H8: /DDR/DQ21 -> /DDR/DQ16
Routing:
- net /DDR/A8: track 0.00 -> 88.1 mm, vias 0 -> 3
- net /DDR/A13: track 0.00 -> 86.2 mm, vias 0 -> 3
- net /DDR/A7: track 0.00 -> 85.2 mm, vias 0 -> 3
- net /DDR/A5: track 0.00 -> 85.0 mm, vias 0 -> 3
- net /DDR/A2: track 0.00 -> 84.5 mm, vias 0 -> 4
- net /DDR/DDR_BA0: track 0.00 -> 83.7 mm, vias 0 -> 4
- net /DDR/A6: track 0.00 -> 83.4 mm, vias 0 -> 4
- net /DDR/A4: track 0.00 -> 83.4 mm, vias 0 -> 4
- net /DDR/A3: track 0.00 -> 83.2 mm, vias 0 -> 3
- net /DDR/A1: track 0.00 -> 82.9 mm, vias 0 -> 4
- net /DDR/A11: track 0.00 -> 81.5 mm, vias 0 -> 4
- net /DDR/DDR_BA2: track 0.00 -> 81.5 mm, vias 0 -> 4
- net /DDR/A9: track 0.00 -> 81.2 mm, vias 0 -> 3
- net /DDR/A0: track 0.00 -> 80.8 mm, vias 0 -> 4
- net /DDR/~DDR_RESET~: track 0.00 -> 80.4 mm, vias 0 -> 3
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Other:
- net class DDR_DIFF_G2 added: clearance 0.15, trace_width 0.17, via_dia 0.4, via_drill 0.2
- net class DDR_GROUP_1 added: clearance 0.1, trace_width 0.14, via_dia 0.4, via_drill 0.2
- net class DDR_GROUP_2 added: clearance 0.1, trace_width 0.205, via_dia 0.4, via_drill 0.2
- net class DDR_GROUP_3 added: clearance 0.1, trace_width 0.205, via_dia 0.4, via_drill 0.2
- net class DDR_GROUP_4 added: clearance 0.1, trace_width 0.205, via_dia 0.4, via_drill 0.2
- net class DDR_GROUP_5 added: clearance 0.1, trace_width 0.14, via_dia 0.4, via_drill 0.2
- net class PWR_FPGA added: clearance 0.1, trace_width 0.3, via_dia 0.4, via_drill 0.2

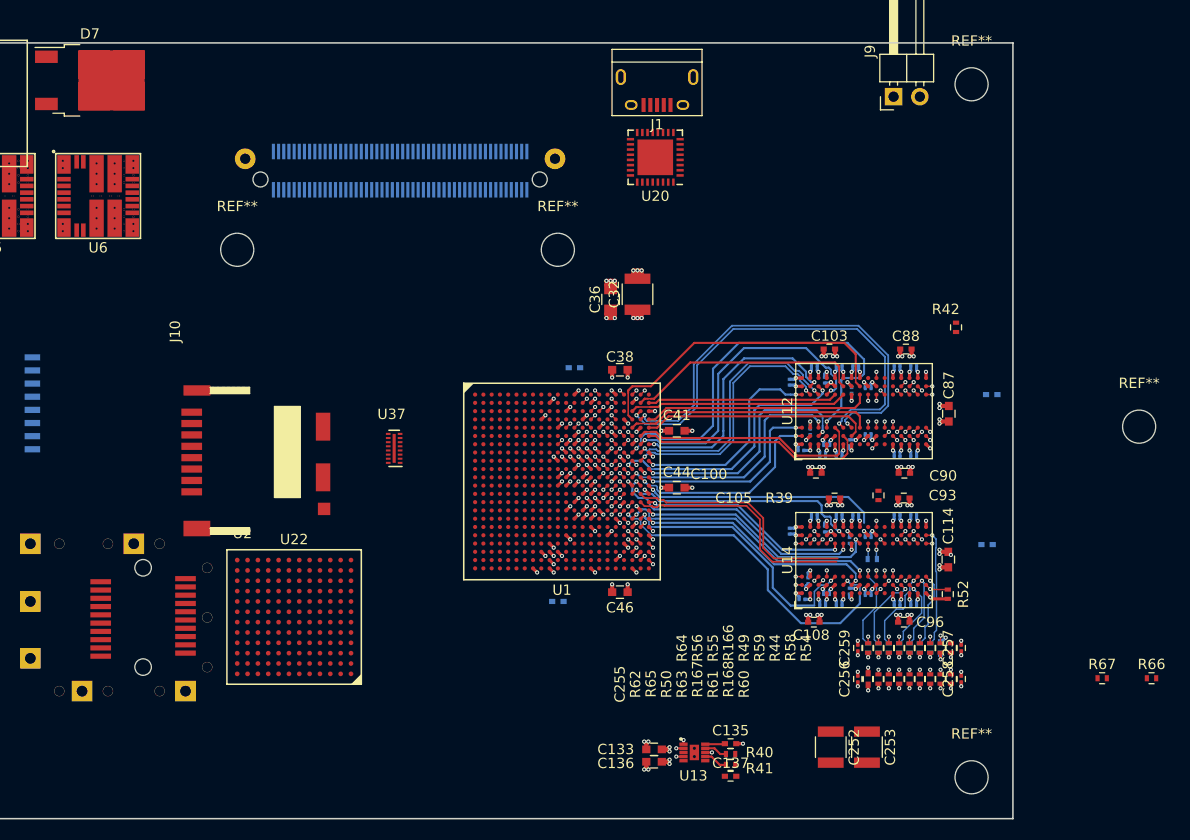
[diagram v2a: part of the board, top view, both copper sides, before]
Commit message: Connected V_TT and V_Ref. Needs to be connected to 5V.
DDR Traces are still not length matched. V_DDR supply is missing.
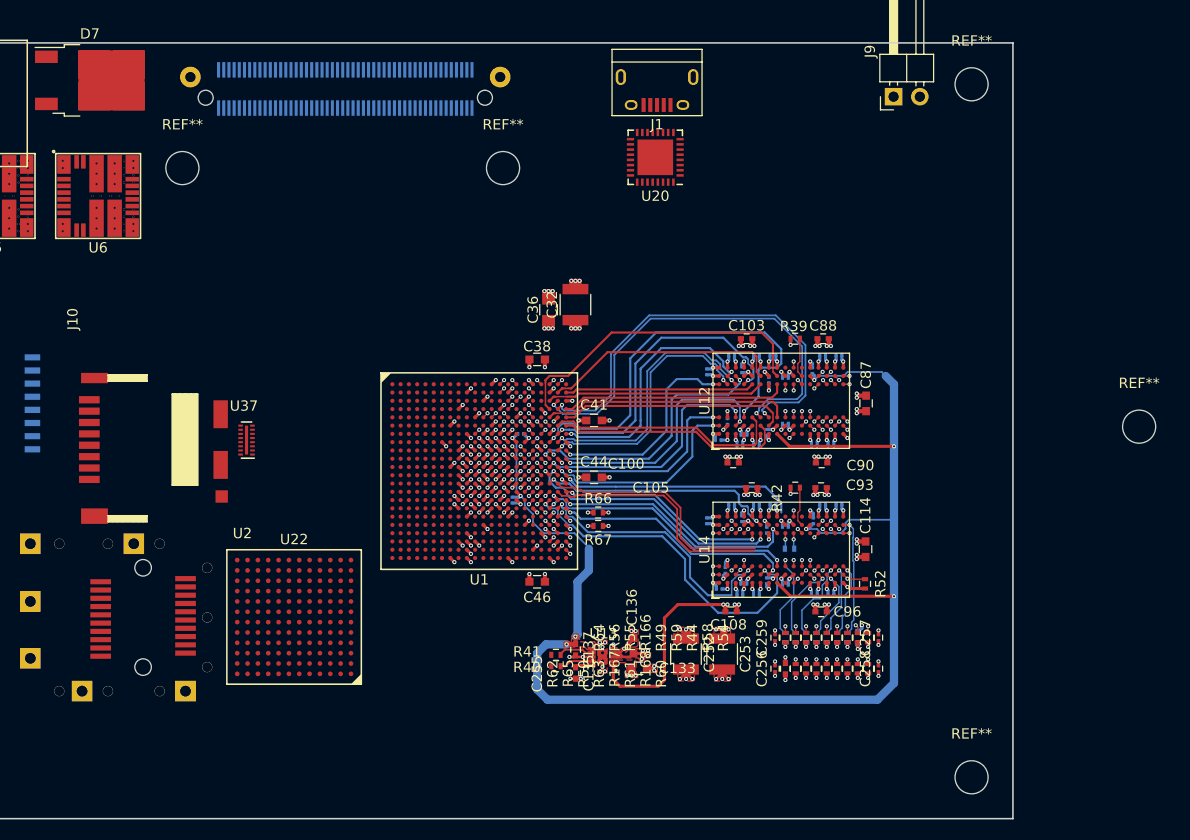
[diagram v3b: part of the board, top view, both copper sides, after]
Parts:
- C131, C138, C139, C140: footprint Capacitors_SMD:C_0402 -> Capacitors_SMD:C_0201
- moved R66 55.8 mm to (149.9, 105.4)
- moved R67 50.9 mm to (149.9, 106.7), turned to 180 degrees
- moved R42 22.0 mm to (168.9, 103.0), turned to 180 degrees
- moved R40 20.0 mm to (145.8, 119.2), turned to 180 degrees
- moved C137 19.3 mm to (147.7, 118.7), turned to 270 degrees
- moved R41 18.9 mm to (145.8, 120.3), turned to 0 degrees
- moved C138 17.5 mm to (170.6, 91.7), turned to 90 degrees
- moved R39 17.2 mm to (168.9, 88.6), turned to 180 degrees
- moved C131 17.0 mm to (170.7, 106.2), turned to 90 degrees
- moved C252 16.6 mm to (158.4, 119.1)
- moved C253 16.6 mm to (161.9, 119.1)
- moved C135 16.5 mm to (147.7, 120.9), turned to 270 degrees
- moved U37 14.3 mm to (115.9, 98.4)
- moved U13 12.8 mm to (150.3, 119.4), turned to 90 degrees
- moved C136 11.4 mm to (153.3, 118.3), turned to 270 degrees
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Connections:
- U13 pad PAD: Net-(U13-PadPAD) -> GND
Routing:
- net /DDR/VREF: track 1.13 -> 144.5 mm, vias 2 -> 8
- net GND: track 105.3 -> 133.5 mm, vias 132 -> 164
- net VCCO_DDR: track 73.1 -> 92.6 mm, vias 78 -> 79
- net /DDR/VTT: track 14.9 -> 30.2 mm, vias 24 -> 33
- net Net-(R66-Pad1): track 0.00 -> 11.9 mm, vias 0 -> 2
- net /DDR/A14: track 77.8 -> 88.8 mm, vias 3 -> 4
- net Net-(R67-Pad2): track 0.00 -> 10.9 mm, vias 0 -> 2
- net VCCO_34: track 1.13 -> 7.92 mm, vias 2 -> 14
- net +1V0: track 5.09 -> 9.05 mm, vias 9 -> 16
- net Net-(R39-Pad1): track 0.00 -> 3.85 mm
- net Net-(R42-Pad1): track 0.00 -> 3.85 mm
- net /DDR/~DDR_RESET~: track 80.4 -> 78.3 mm
- net /DDR/A13: track 86.2 -> 84.7 mm
- net /DDR/A3: track 83.2 -> 81.8 mm
- net /DDR/A7: track 85.2 -> 83.9 mm
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- added copper zone on F.Cu, net /DDR/VREF
- added copper zone on F.Cu, net /DDR/VTT
- added copper zone on PWR4.Cu, net /DDR/VTT
- added copper zone on F.Cu, net GND
- added copper zone on F.Cu, net VCCO_DDR
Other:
- board text added: "TODO: Attach 5V"
- board text removed: "VDD"
- board text removed: "VDDQ"

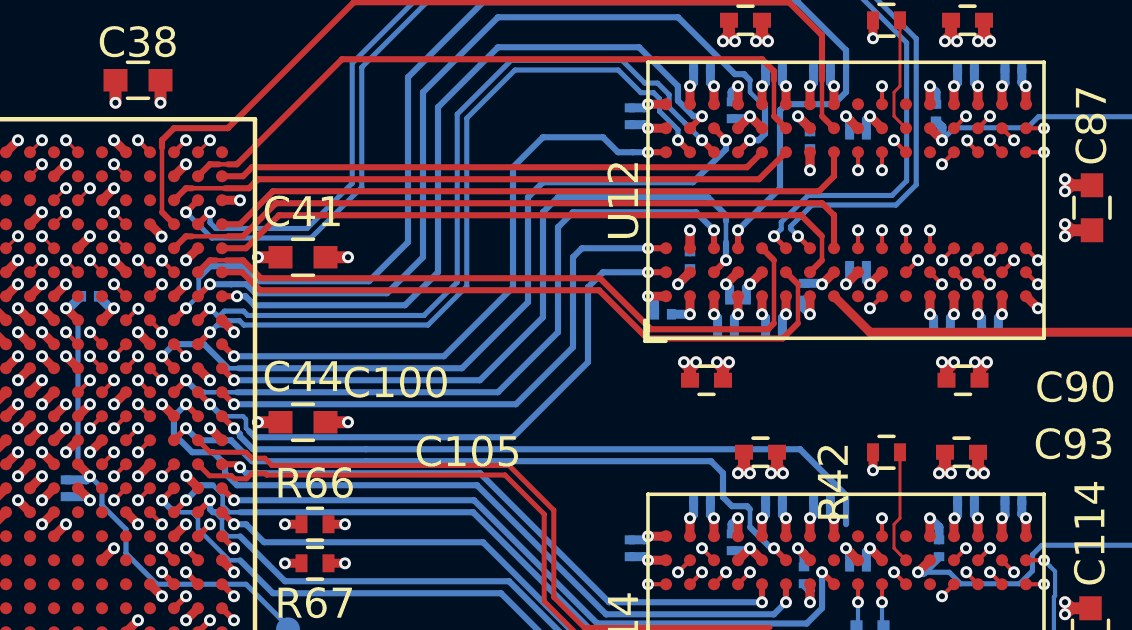
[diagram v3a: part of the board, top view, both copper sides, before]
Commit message: DDR3 Addressbus is length matched.
Databus is not length matched yet. Also DQS3 still needs to be connected. I have no good Idea for that, yet.
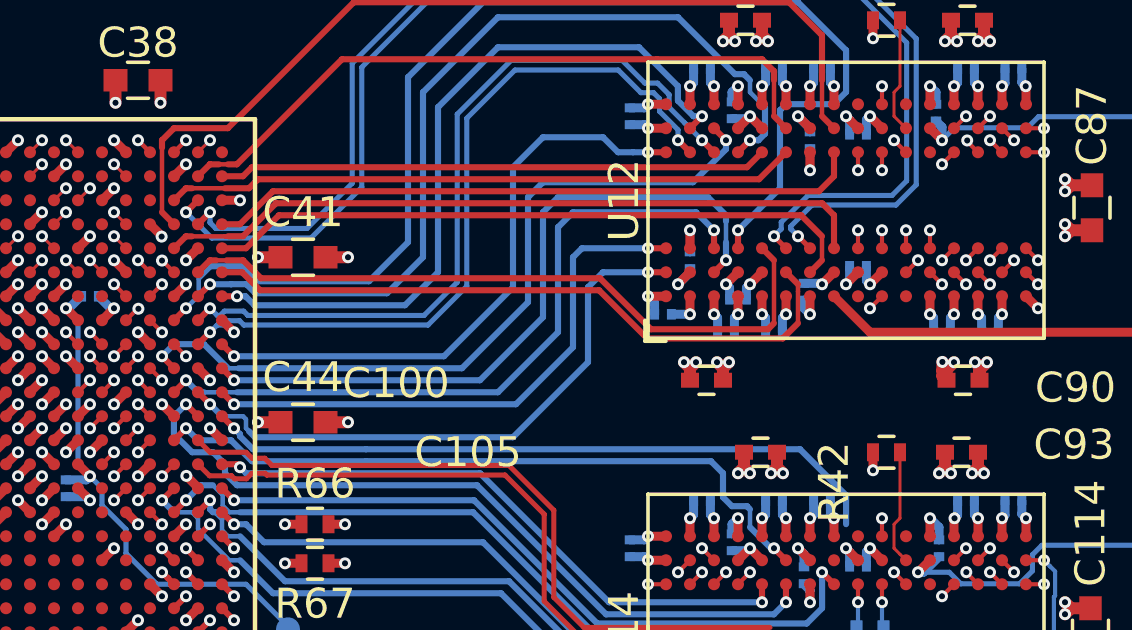
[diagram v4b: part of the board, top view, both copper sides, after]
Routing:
- net /DDR/A10: track 71.6 -> 92.7 mm
- net /DDR/DDR_CKE: track 70.2 -> 87.5 mm
- net /DDR/A12: track 73.9 -> 91.2 mm
- net /DDR/DDR_CLK_N: track 62.4 -> 79.5 mm
- net /DDR/~DDR_CAS~: track 71.8 -> 88.8 mm
- net /DDR/DDR_CLK_P: track 62.6 -> 79.0 mm
- net /DDR/A4: track 83.6 -> 99.7 mm
- net /DDR/~DDR_RAS~: track 70.7 -> 85.9 mm
- net /DDR/DDR_BA1: track 76.8 -> 91.9 mm
- net /DDR/DDR_ODT: track 73.8 -> 85.5 mm
- net /DDR/DDR_BA2: track 80.9 -> 92.5 mm
- net /DDR/A0: track 80.4 -> 91.4 mm
- net /DDR/A6: track 83.3 -> 94.2 mm
- net /DDR/A11: track 82.3 -> 92.9 mm
- net /DDR/A2: track 83.4 -> 93.7 mm
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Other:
- board text added: "TODO: Connect DQS3"
